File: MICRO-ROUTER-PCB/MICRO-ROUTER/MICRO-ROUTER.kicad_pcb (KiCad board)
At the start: 2 copper layers, 85 x 54 mm, 77 parts, among them J2 USB_A, J3 USB_C_Receptacle_USB2.0_16P, J4 Battery Connector, J5 SPI Header, J6 GPIO Header, J7 RJ45 5-2301996-6, Q1 FS8205A, SW2 8Devices Reset, SW3 UART Reset, U1 TP4056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

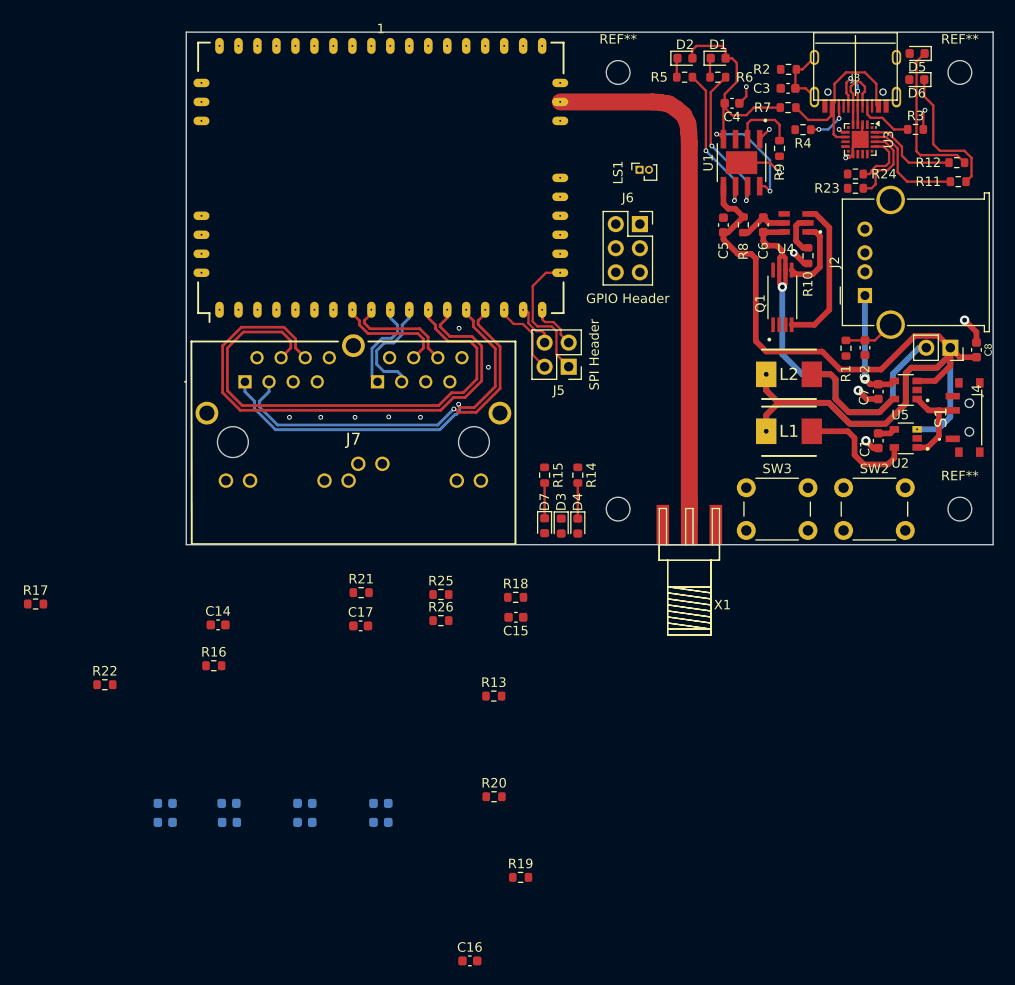
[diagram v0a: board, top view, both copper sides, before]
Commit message: wired power rails
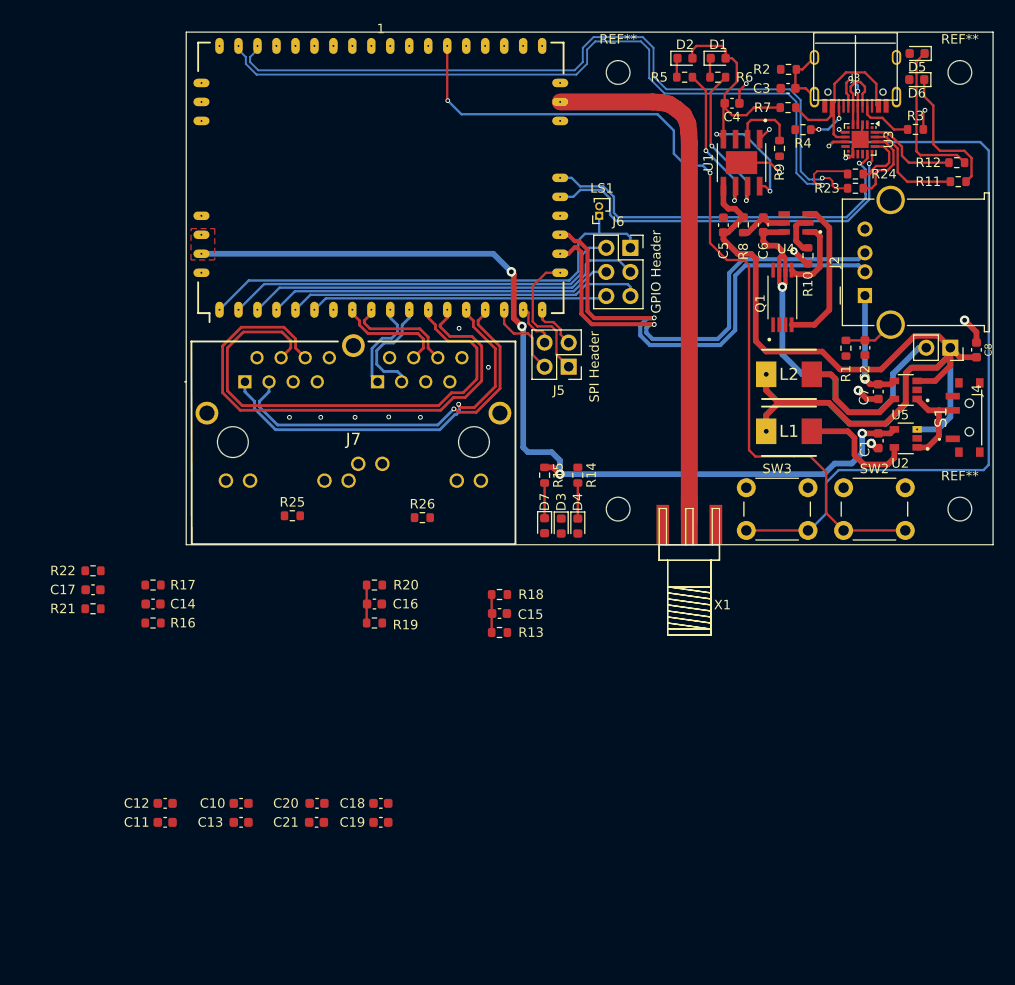
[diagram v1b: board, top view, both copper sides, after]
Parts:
- C10, C11, C12, C13, C18, C19, C20, C21: moved to F.Cu
- moved C16 38.9 mm to (70.3, 193.0), turned to 180 degrees
- moved R19 30.9 mm to (70.3, 195.0)
- moved C17 28.5 mm to (40.7, 191.5), turned to 180 degrees
- moved R21 28.3 mm to (40.7, 193.5)
- moved R20 25.6 mm to (70.3, 191.0)
- moved C11 22.7 mm to (48.3, 216.0), turned to 0 degrees
- moved C12 22.7 mm to (48.3, 214.0), turned to 0 degrees
- moved C18 22.7 mm to (71.0, 214.0), turned to 0 degrees
- moved C19 22.7 mm to (71.0, 216.0), turned to 0 degrees
- moved R25 17.7 mm to (61.7, 183.7)
- moved R17 12.5 mm to (47.0, 191.0), turned to 180 degrees
- moved R22 12.1 mm to (40.7, 189.5)
- moved R26 11.0 mm to (75.4, 183.9)
- moved C20 9.28 mm to (64.3, 214.0), turned to 0 degrees
- moved C21 9.17 mm to (64.2, 216.0), turned to 0 degrees
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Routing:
- net +3.3V: track 2.68 -> 99.5 mm, vias 1 -> 5
- net Net-(1-RESET): track 0.00 -> 92.5 mm, vias 0 -> 2
- net URAT-TX: track 0.00 -> 83.7 mm, vias 0 -> 1
- net Net-(U3-~{RST}): track 0.00 -> 82.8 mm, vias 0 -> 1
- net URAT-RX: track 0.00 -> 80.8 mm, vias 0 -> 1
- net GPIO 1: track 0.00 -> 51.7 mm
- net USB-A-D-: track 0.00 -> 51.4 mm, vias 0 -> 1
- net USB-A-D+: track 0.00 -> 49.3 mm, vias 0 -> 1
- net GPIO 2: track 0.00 -> 42.6 mm
- net GPIO 3: track 0.00 -> 42.6 mm
- net RTS: track 0.00 -> 41.4 mm, vias 0 -> 1
- net CTS: track 0.00 -> 41.2 mm, vias 0 -> 1
- net GPIO 5: track 0.00 -> 37.5 mm
- net GPIO 4: track 0.00 -> 36.4 mm
- net GPIO 6: track 0.00 -> 31.3 mm
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- added copper zone on F.Cu, net +3.3V

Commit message: wired cap array for rj45
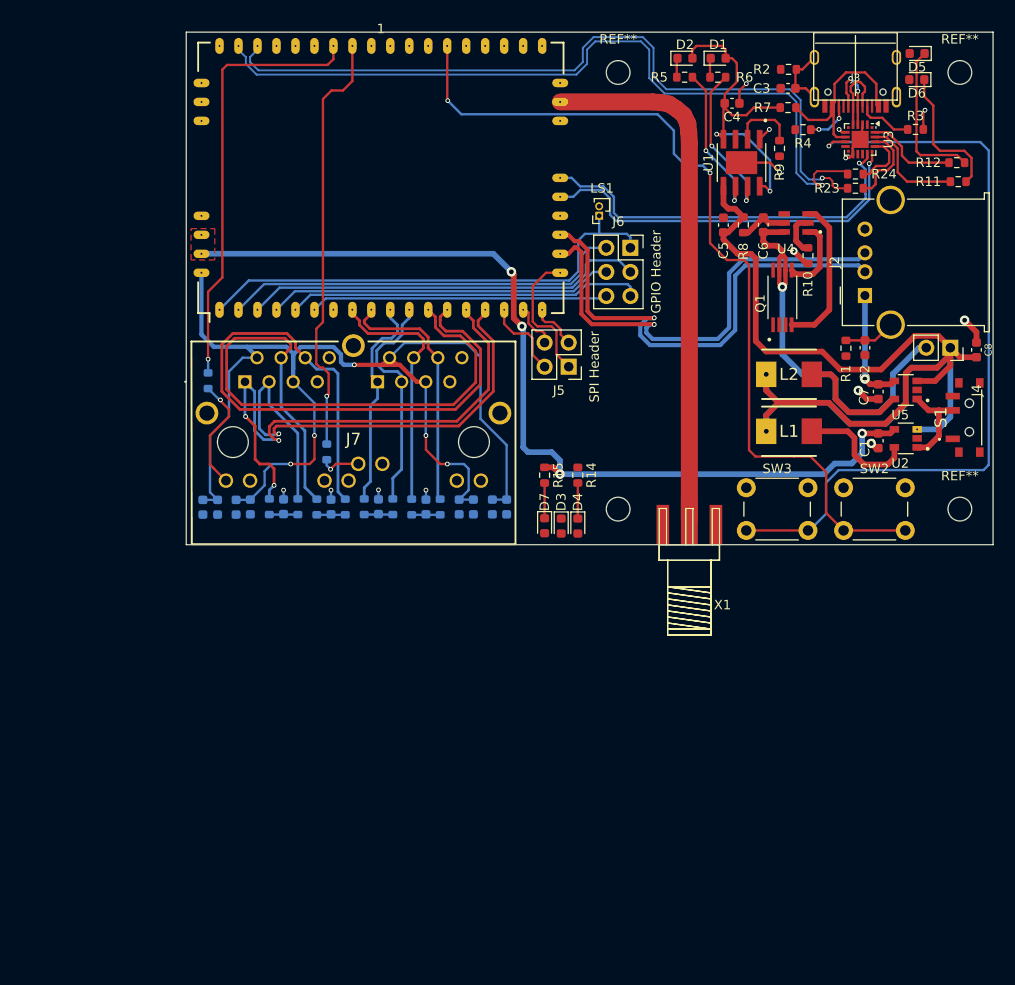
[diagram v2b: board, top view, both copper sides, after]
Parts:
- C10, C11, C12, C13, C14, C15, C16, C17, C18, C19, C20, C21, R13, R16, R17, R18, R19, R20, R21, R22, R25, R26: moved to B.Cu
- moved C11 47.9 mm to (82.8, 182.8), turned to 90 degrees
- moved C12 47.6 mm to (84.2, 182.8), turned to 90 degrees
- moved C13 40.4 mm to (79.2, 182.8), turned to 90 degrees
- moved C10 39.7 mm to (80.8, 182.8), turned to 90 degrees
- moved C19 36.5 mm to (55.8, 182.8), turned to 90 degrees
- moved C21 35.3 mm to (52.2, 182.8), turned to 90 degrees
- moved C18 34.1 mm to (57.2, 182.8), turned to 90 degrees
- moved R21 33.4 mm to (72.3, 182.8), turned to 90 degrees
- moved C20 32.9 mm to (53.8, 182.8), turned to 90 degrees
- moved C17 31.3 mm to (70.8, 182.8), turned to -90 degrees
- moved R22 29.4 mm to (69.2, 182.8), turned to 90 degrees
- moved R13 23.4 mm to (64.2, 182.8), turned to 90 degrees
- moved C15 21.0 mm to (65.8, 182.8), turned to -90 degrees
- moved R16 19.6 mm to (62.2, 182.8), turned to 90 degrees
- moved R18 18.7 mm to (67.2, 182.8), turned to 90 degrees
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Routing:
- net +2v: track 0.00 -> 127.3 mm, vias 0 -> 5
- net Net-(1-LED2): track 0.00 -> 46.1 mm, vias 0 -> 1
- net Net-(1-LED3): track 0.00 -> 45.1 mm, vias 0 -> 1
- net ETH0-TX+: track 42.0 -> 59.1 mm, vias 1 -> 3
- net ETH0-RX-: track 56.7 -> 73.4 mm
- net ETH0-TX-: track 40.7 -> 56.6 mm
- net ETH0-RX+: track 53.3 -> 68.9 mm
- net ETH1-RX-: track 11.6 -> 26.6 mm
- net ETH1-RX+: track 11.6 -> 26.6 mm
- net ETH1-TX+: track 9.84 -> 22.8 mm
- net ETH1-TX-: track 11.5 -> 24.2 mm
- net ETH0-LED: track 0.00 -> 12.2 mm, vias 0 -> 1
- net ETH1-LED: track 0.00 -> 4.93 mm, vias 0 -> 1
- net GND: track 23.2 -> 27.2 mm, vias 9 -> 13
- net Net-(C17-Pad2): track 0.00 -> 3.00 mm
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
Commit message: finished layout
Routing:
- net Net-(1-LED0): track 0.00 -> 71.5 mm, vias 0 -> 3
- net Net-(D2-K): track 2.03 -> 67.0 mm, vias 0 -> 2
- net +3.3V: track 99.5 -> 159.5 mm, vias 5 -> 6
- net Net-(D1-A): track 34.9 -> 76.6 mm, vias 2 -> 4
- net GND: track 27.2 -> 29.1 mm, vias 13 -> 34
- added copper zone on B.Cu, net GND
- added copper zone on F.Cu, net GND

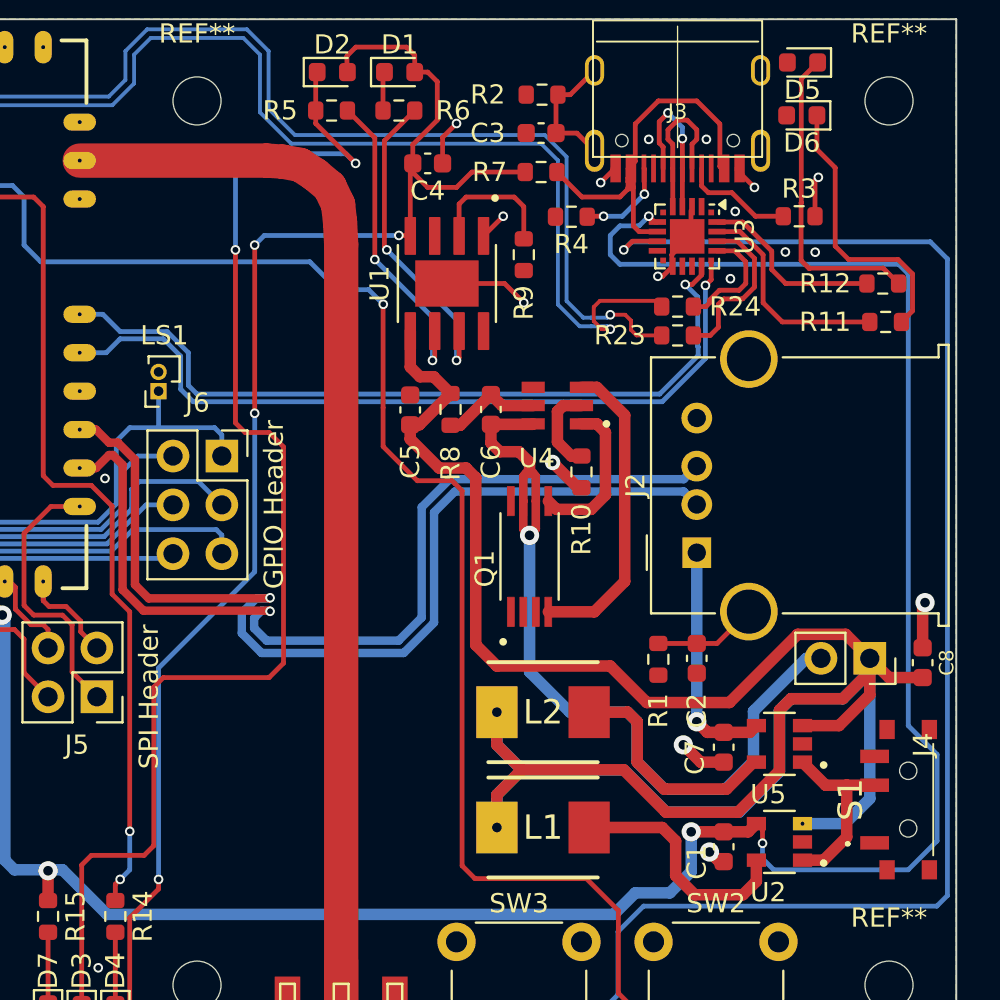
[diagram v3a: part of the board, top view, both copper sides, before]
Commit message: -Finished layout -Added GND vias -Added rendering photo -3d model association
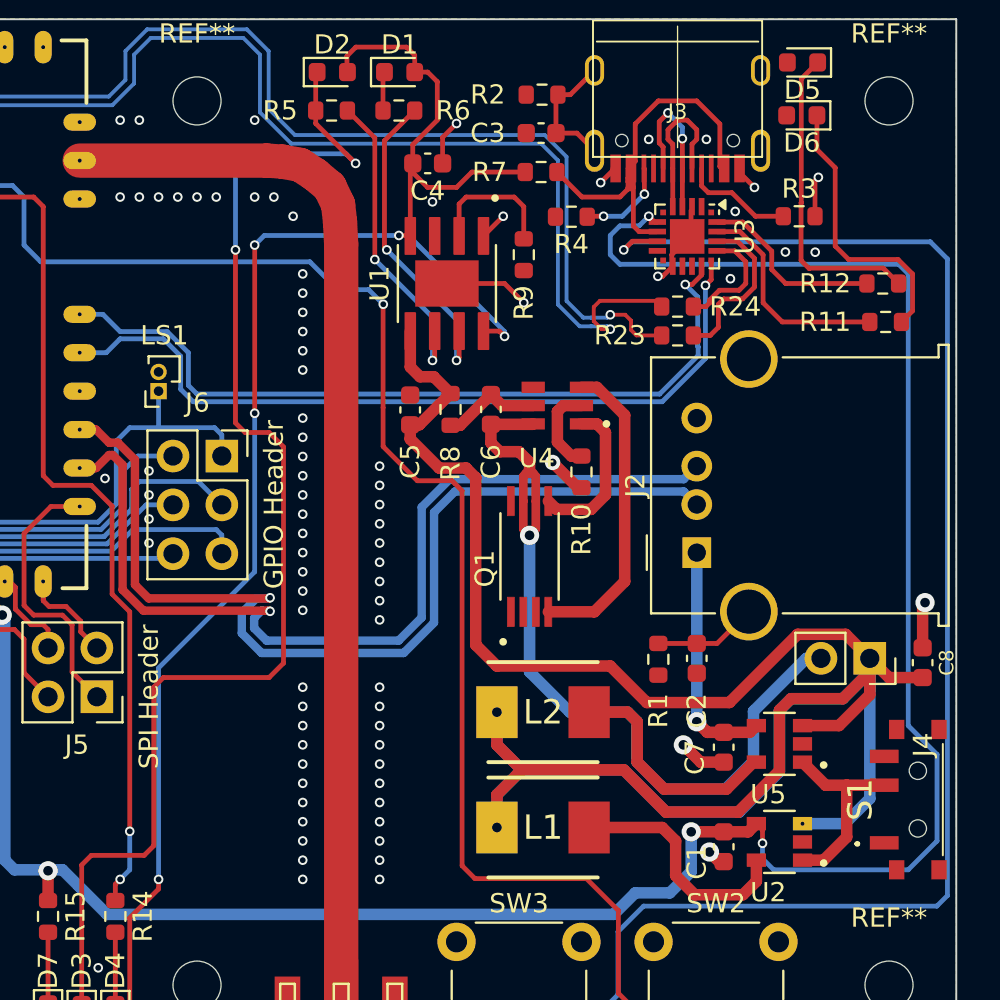
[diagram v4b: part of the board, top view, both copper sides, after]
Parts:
- U4: value DW01A -> SOT95P280X145-6N
- moved S1 0.50 mm to (133.5, 173.3)
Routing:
- net Net-(D1-A): track 76.6 -> 85.6 mm, vias 4 -> 5
- net V-UNREG SW: track 9.74 -> 10.2 mm
- net GND: vias 34 -> 99

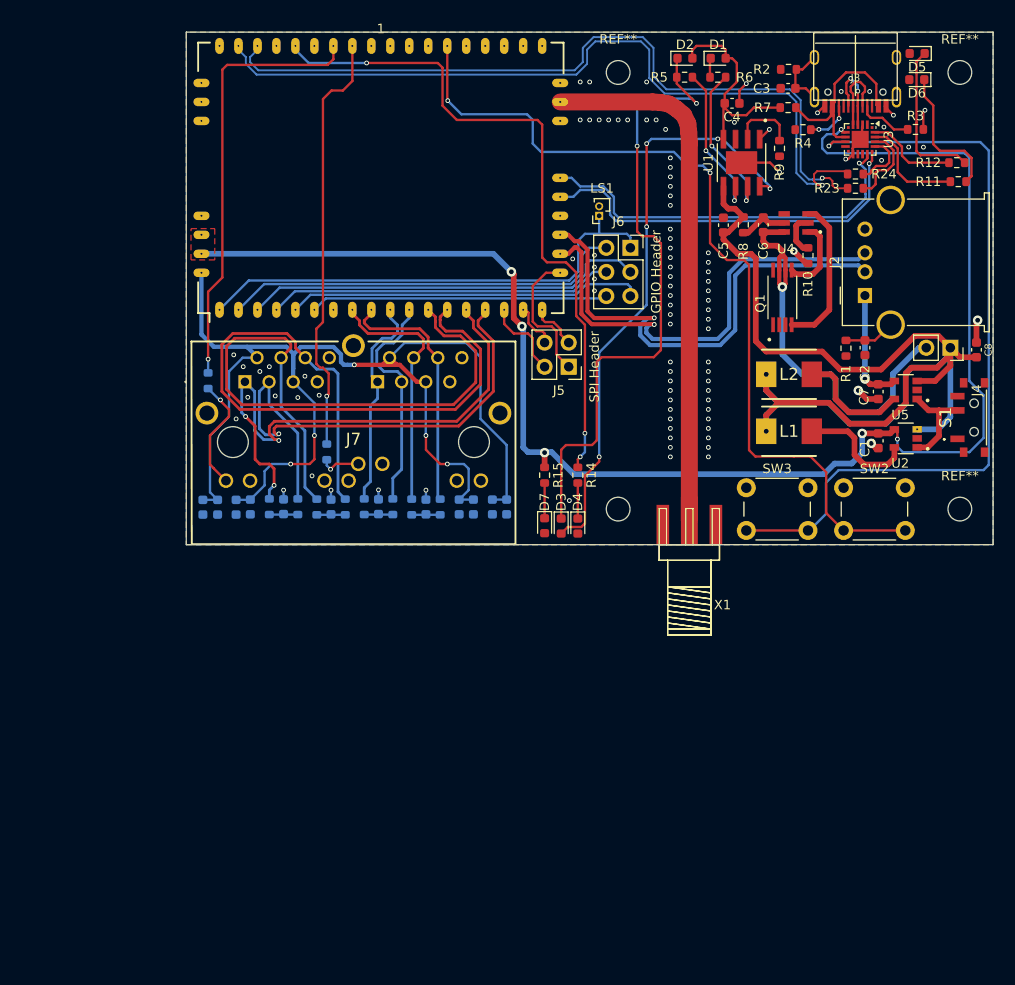
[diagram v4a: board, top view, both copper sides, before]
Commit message: - fixed skew - fixed GND islands - moved some dif pairs to reduce loss - added silk
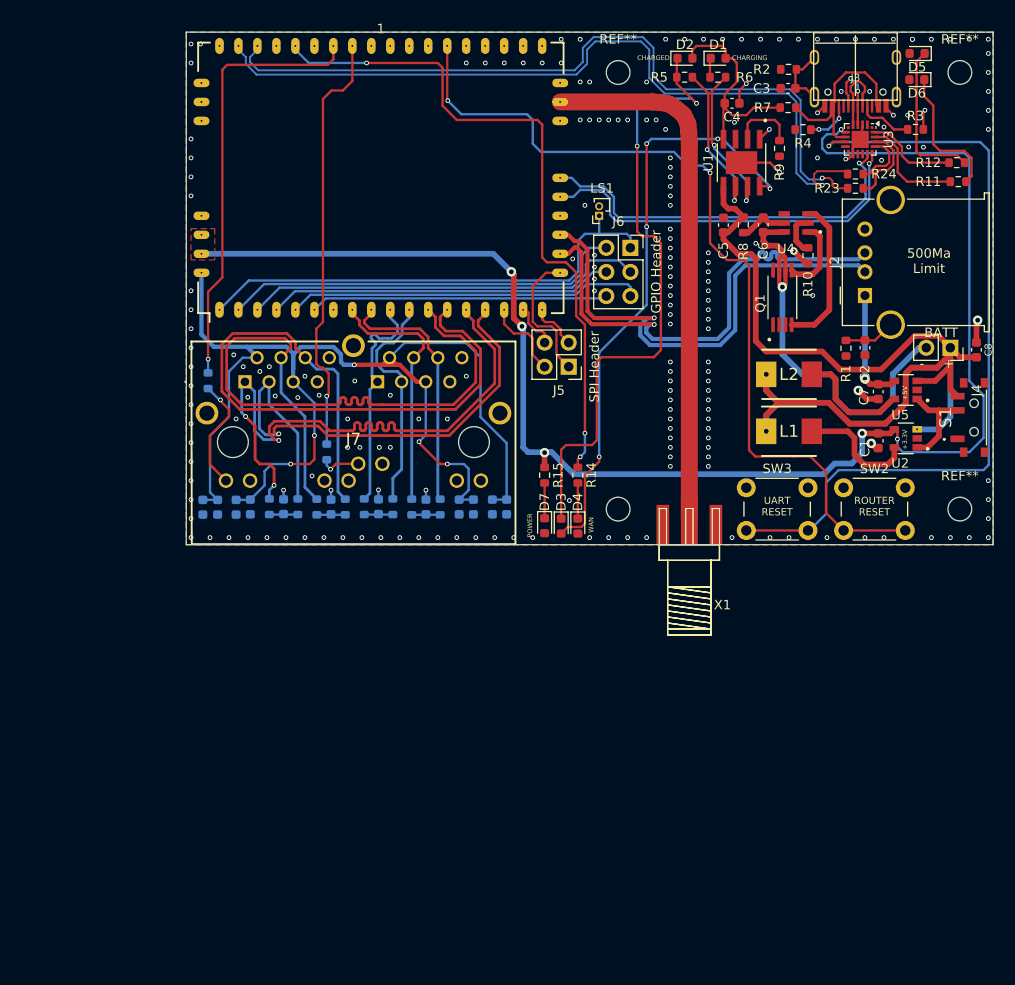
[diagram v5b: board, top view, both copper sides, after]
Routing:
- net ETH0-TX+: track 59.4 -> 65.9 mm
- net V-UNREG: track 129.0 -> 132.5 mm
- net ETH0-RX+: track 68.9 -> 72.1 mm
- net USB-A-D+: track 49.4 -> 51.4 mm
- net ETH1-TX+: track 22.8 -> 24.3 mm
- net ETH0-TX-: track 56.6 -> 58.0 mm
- net +2v: track 127.3 -> 127.9 mm
- net GND: vias 99 -> 204
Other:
- board text added: "+"
- board text added: "+3.3V"
- board text added: "+5V"
- board text added: "-"
- board text added: "500Ma Limit"
- board text added: "BATT"
- board text added: "CHARGED"
- board text added: "CHARGING"
- board text added: "POWER"
- board text added: "ROUTER RESET"
- board text added: "UART RESET"
- board text added: "WAN"

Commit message: -added decrotive silk -ran drc -fixed small layout errors
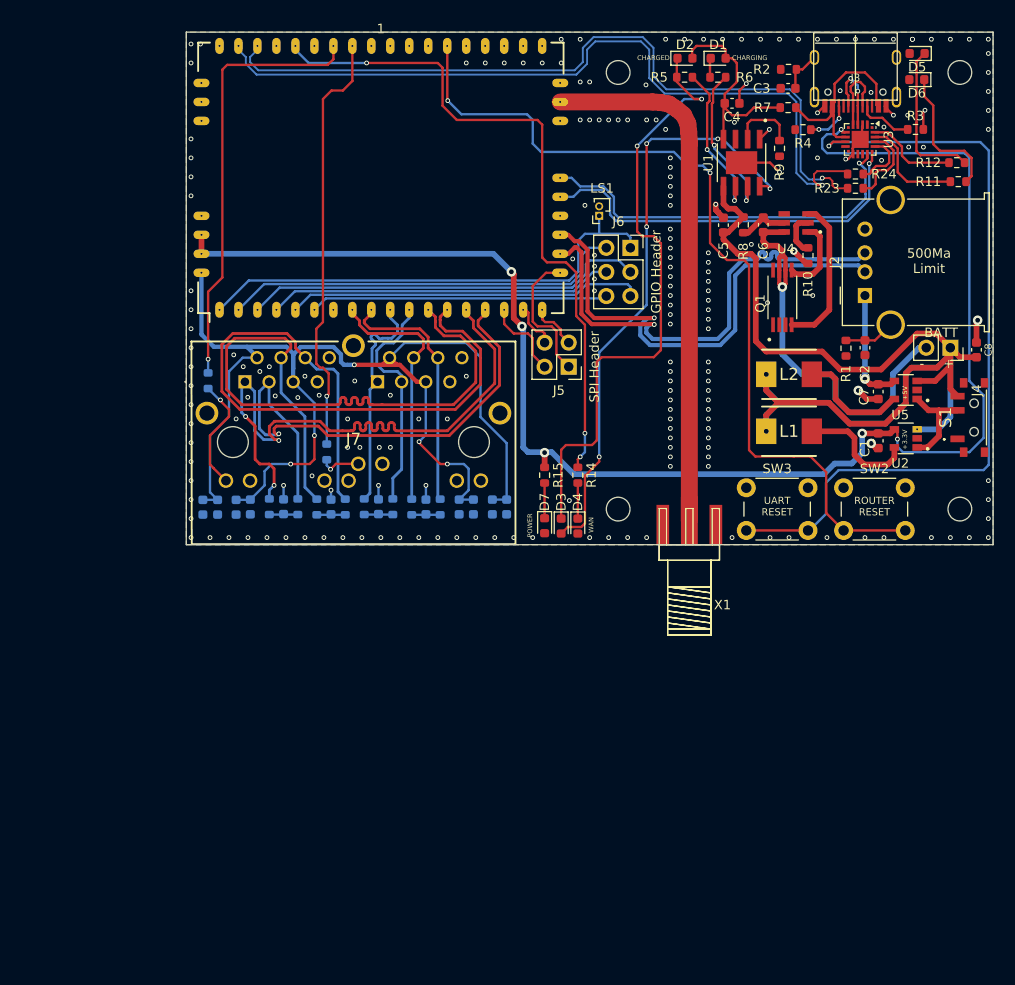
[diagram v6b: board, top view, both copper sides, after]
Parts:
- added G***: LOGO, Custom-Silk:Cyberpunk-Backround-Micro-Router, B.Cu at (91.5, 162.5)
- U4: value SOT95P280X145-6N -> DW01A
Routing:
- net GND: track 29.1 -> 32.3 mm, vias 204 -> 206
- net Net-(J3-SHIELD): track 6.85 -> 4.47 mm
- net Net-(D2-K): track 67.0 -> 64.9 mm
- net +3.3V: track 159.5 -> 161.5 mm
- net (no net): vias 1 -> 0
- removed copper zone on F.Cu, net +3.3V

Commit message: -added output files for rev00
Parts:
- added G***: LOGO, Custom-Silk:LOGO, F.Cu at (71.0, 148.5)
